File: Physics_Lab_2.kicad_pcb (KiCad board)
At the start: 2 copper layers, 60.8 x 57 mm, 9 parts, among them J1 USB_C, U1 MCP73871, U2 S2B-PH-K-S-GW

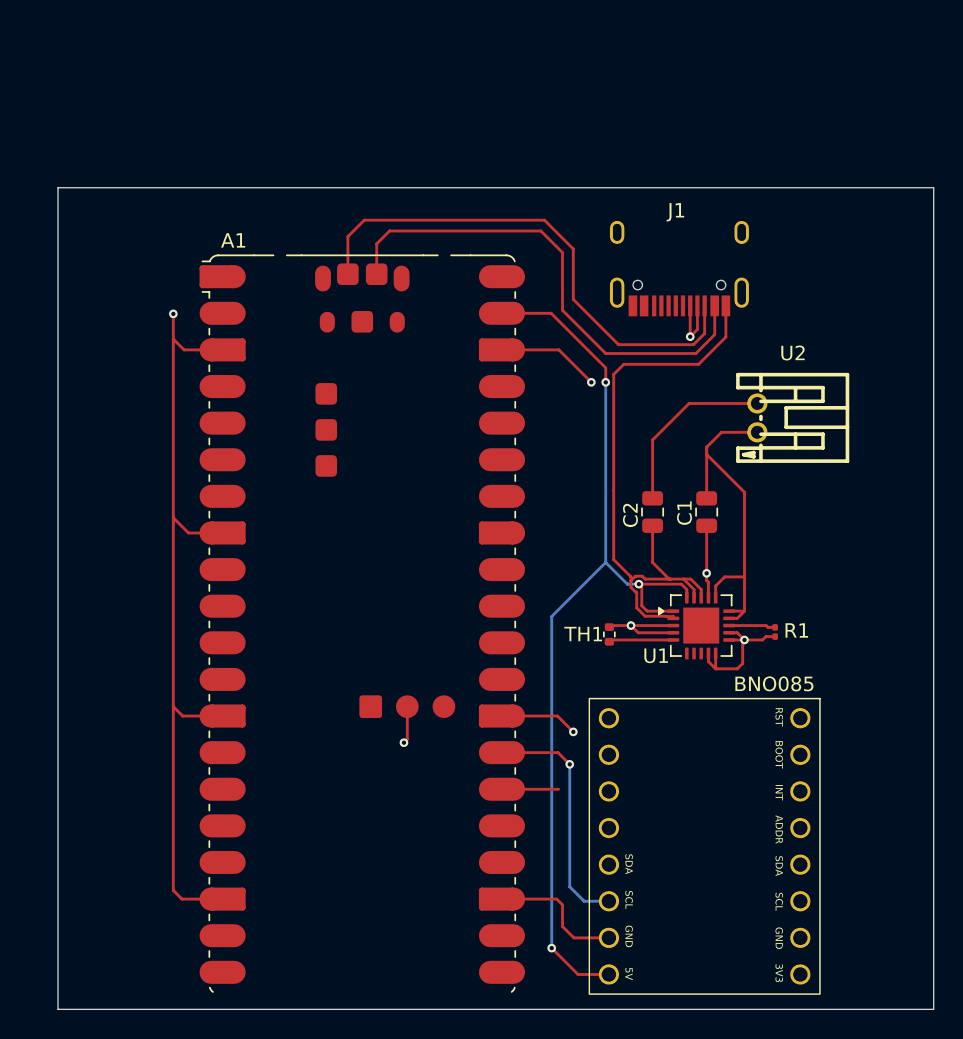
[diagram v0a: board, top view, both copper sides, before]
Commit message: Add mounting holes and remove errors
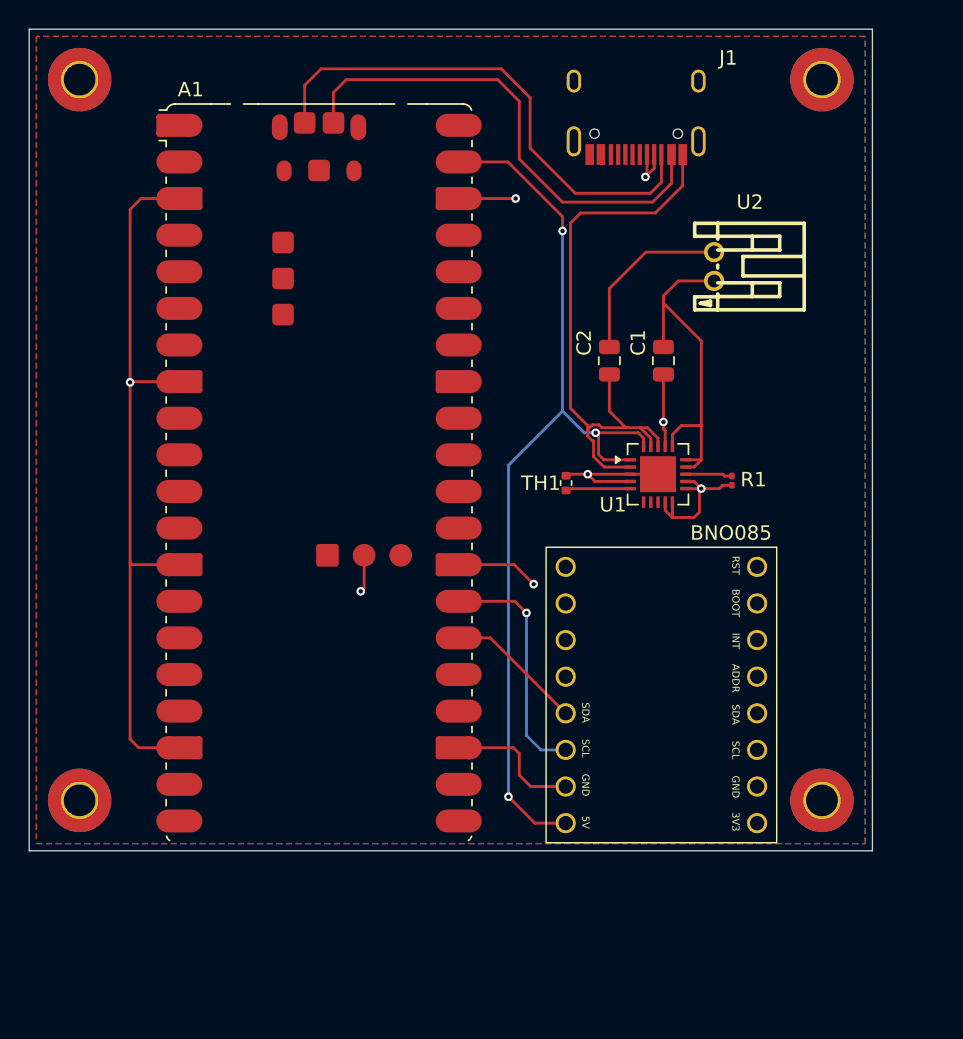
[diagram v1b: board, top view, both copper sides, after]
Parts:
- added REF**: MountingHole_2.2mm_M2_Pad_TopBottom, MountingHole:MountingHole_2.2mm_M2_Pad_TopBottom, F.Cu at (155.0, 53.5)
- added REF**: MountingHole_2.2mm_M2_Pad_TopBottom, MountingHole:MountingHole_2.2mm_M2_Pad_TopBottom, F.Cu at (155.0, 103.5)
- added REF**: MountingHole_2.2mm_M2_Pad_TopBottom, MountingHole:MountingHole_2.2mm_M2_Pad_TopBottom, F.Cu at (103.5, 103.5)
- added REF**: MountingHole_2.2mm_M2_Pad_TopBottom, MountingHole:MountingHole_2.2mm_M2_Pad_TopBottom, F.Cu at (103.5, 53.5)
- moved A1 10.9 mm to (120.1, 80.8)
- moved BNO085_Halley1 10.9 mm to (150.5, 87.3)
- moved C1 10.9 mm to (144.0, 73.0)
- moved C2 10.9 mm to (140.2, 73.0)
- moved J1 10.9 mm to (142.1, 51.0)
- moved R1 10.9 mm to (148.8, 81.3)
- moved TH1 10.9 mm to (137.2, 81.5)
- moved U1 10.9 mm to (143.6, 80.9)
- moved U2 10.9 mm to (147.5, 66.5)
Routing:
- net GND: track 119.9 -> 114.0 mm
- net Net-(A1-GPIO20): track 4.20 -> 9.86 mm
- added copper zone on B.Cu, net GND
- added copper zone on F.Cu, net GND
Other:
- board size 60.8 x 57 mm -> 58.5 x 57 mm
